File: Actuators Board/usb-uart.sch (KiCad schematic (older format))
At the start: 15 parts, among them J3 USB_C_Receptacle_USB2.0, U3 INTERFACE-CP2102-GMR(QFN28)

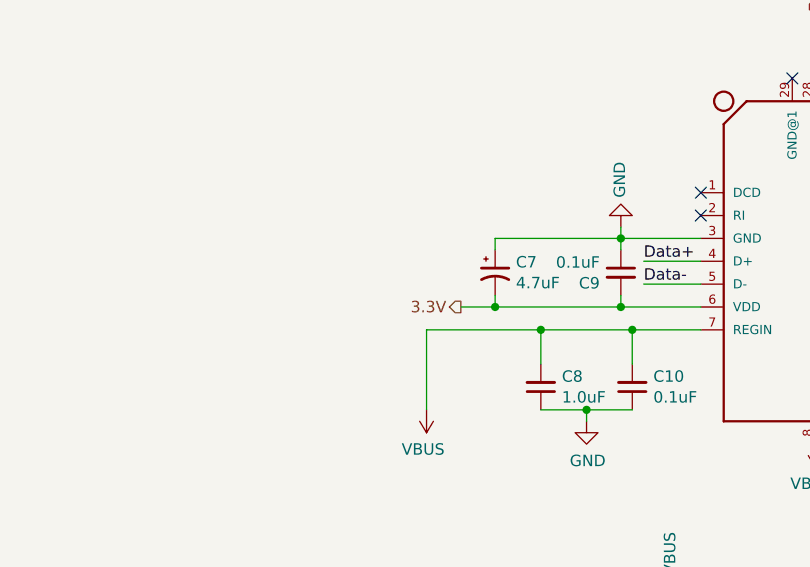
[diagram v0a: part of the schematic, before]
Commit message: Assigned footprints, changed sense resistor value, added diode to UART
Sense resistor on the buck converter changed from 1.5K to 1.54K to more closely match 6V. Also added a diode on the 3.3V output on the USB-UART converter.
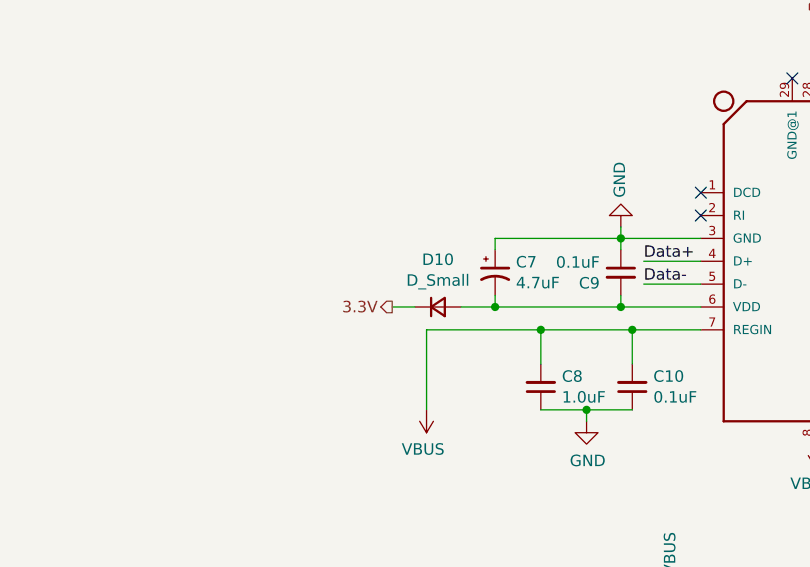
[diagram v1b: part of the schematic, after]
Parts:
- added D10: D_Small, Diode_SMD:D_0805_2012Metric_Castellated, symbol Device:D_Small
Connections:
- net 3.3V: now also D10.1 (K); no longer C7.2, C9.2, U3.6 (VDD)
- new net: C7.2, C9.2, D10.2 (A), U3.6 (VDD)
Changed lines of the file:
@@
 $EndComp
 NoConn ~ 5450 2650
-Text HLabel 3700 2050 0    50   Output ~ 0
+Text HLabel 3400 2050 0    50   Output ~ 0
 3.3V
 $Comp
@@
 	-1   0    0    1
 $EndComp
+$Comp
+L Device:D_Small D10
+U 1 1 61E1C0D8
+P 3600 2050
+F 0 "D10" H 3600 2257 50  0000 C CNN
+F 1 "D_Small" H 3600 2166 50  0000 C CNN
+F 2 "Diode_SMD:D_0805_2012Metric_Castellated" V 3600 2050 50  0001 C CNN
+F 3 "~" V 3600 2050 50  0001 C CNN
+	1    3600 2050
+	1    0    0    -1
+$EndComp
+Wire Wire Line
+	3500 2050 3400 2050
 $EndSCHEMATC
